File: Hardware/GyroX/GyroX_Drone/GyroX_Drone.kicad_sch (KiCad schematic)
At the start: 13 parts, among them J1 USB_C_Receptacle_USB2.0_16P, Q1 PMOS, U1 SPX3819M5-L-3-3

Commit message: USB-UART circuit designed
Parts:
- added C19, C20: 0.1uF, Capacitor_SMD:C_0603_1608Metric, symbol Device:C
- added R8, R9: 1k, Resistor_SMD:R_0603_1608Metric, symbol Device:R
- added U2: CH340K, Package_SO:SSOP-10-1EP_3.9x4.9mm_P1mm_EP2.1x3.3mm, symbol Interface_USB:CH340K
- added U3: 2N7002DW, 2N7002DW:SOT363, symbol 2N7002DW:2N7002DW
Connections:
- net +3.3V: now also C20.1, U2.7 (VCC)
- net D+: now also U2.1 (UD+)
- net D-: now also U2.2 (UD-)
- net GND: now also C19.2, C20.2, U2.11 (GND), U2.3 (GND)
- new net: R9.2, U2.9 (RXD)
- new net: R8.2, U2.8 (TXD)
- new net: C19.1, U2.10 (V3)
- new net DTR: U2.4 (~{DTR}), U3.2 (G1), U3.4 (S2)
- new net EN: U3.6 (D1)
- new net IO0: U3.3 (D2)
- new net RTS: U2.6 (~{RTS}), U3.1 (S1), U3.5 (G2)
- new net RX: R9.1
- new net TX: R8.1
- no-connect marks 2 -> 3
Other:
- note added: "USB - UART CIRCUIT"
- note added: "USB-C POWER IN CIRCUIT"

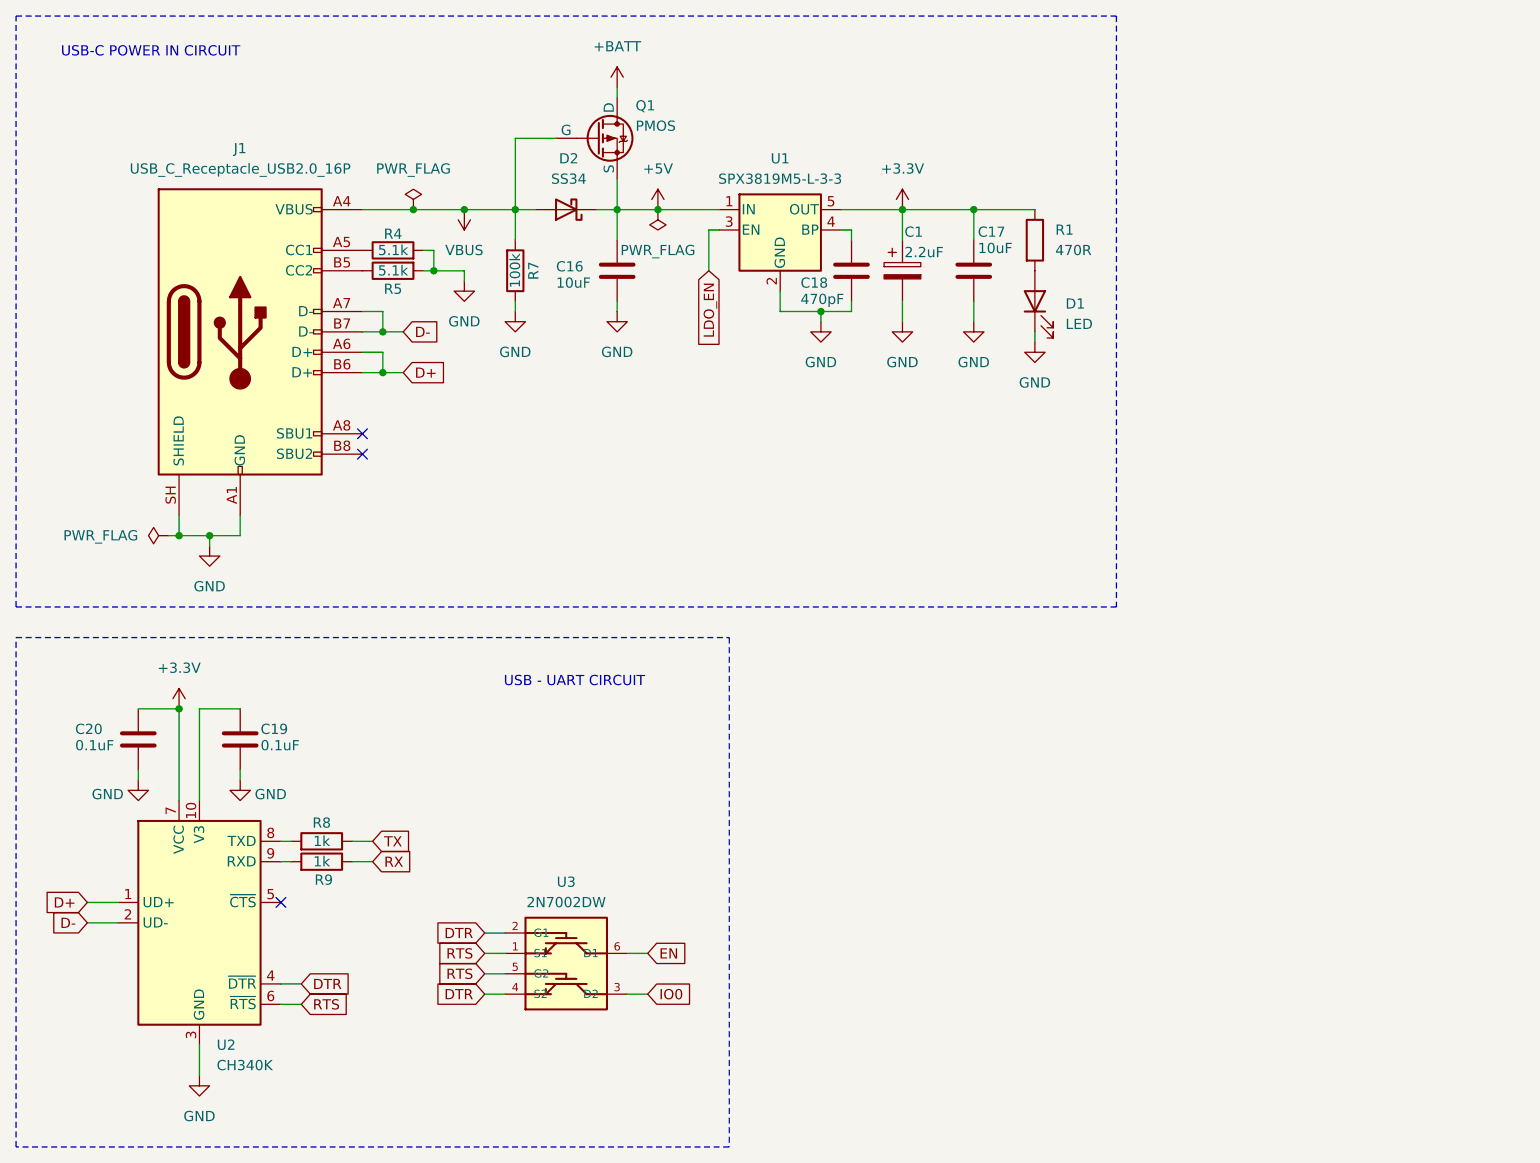
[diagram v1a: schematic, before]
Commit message: Battery charging circuit designed
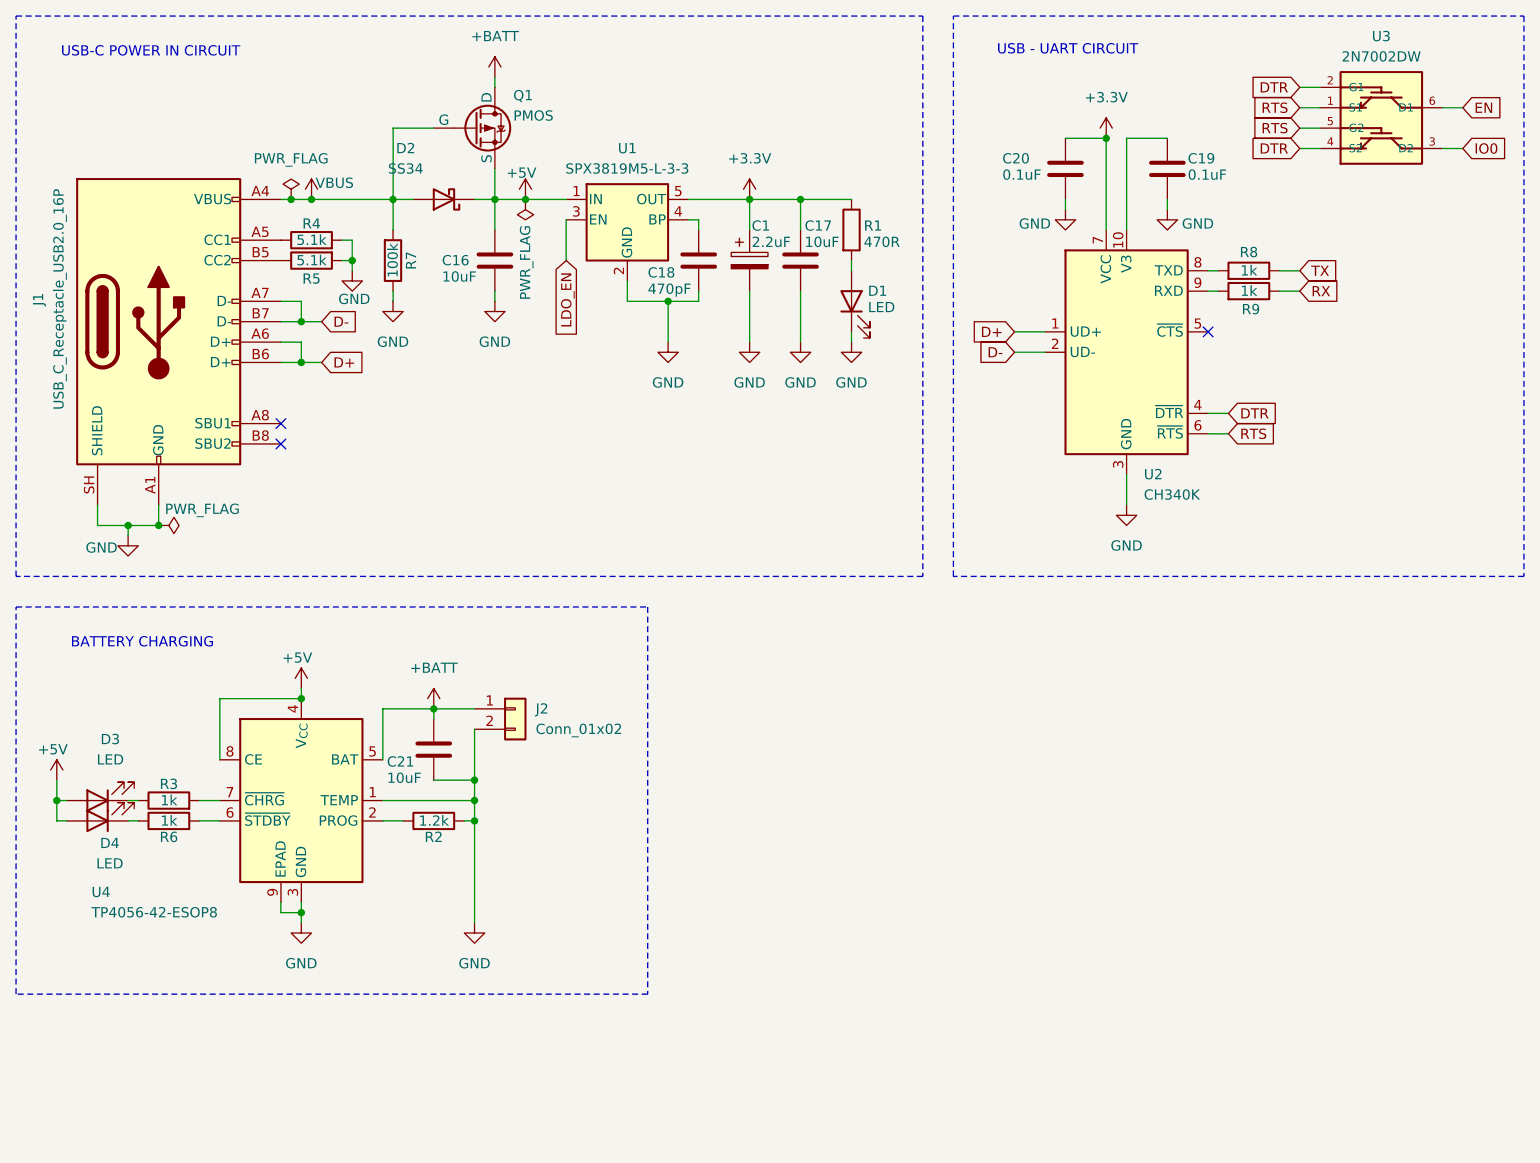
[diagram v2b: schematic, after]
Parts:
- added C21: 10uF, Capacitor_SMD:C_0603_1608Metric, symbol Device:C
- added D3, D4: LED, symbol Device:LED
- added J2: Conn_01x02, symbol Connector_Generic:Conn_01x02
- added R2: 1.2k, symbol Device:R
- added R3, R6: 1k, symbol Device:R
- added U4: TP4056-42-ESOP8, Package_SO:SOIC-8-1EP_3.9x4.9mm_P1.27mm_EP2.41x3.3mm_ThermalVias, symbol Battery_Management:TP4056-42-ESOP8
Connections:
- net +5V: now also D3.2 (A), D4.2 (A), U4.4 (V_{CC}), U4.8 (CE)
- net +BATT: now also C21.1, J2.1 (Pin_1), U4.5 (BAT)
- net GND: now also C21.2, J2.2 (Pin_2), R2.2, U4.1 (TEMP), U4.3 (GND), U4.9 (EPAD)
- new net: R2.1, U4.2 (PROG)
- new net: D3.1 (K), R3.1
- new net: R3.2, U4.7 (~{CHRG})
- new net: D4.1 (K), R6.1
- new net: R6.2, U4.6 (~{STDBY})
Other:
- note added: "BATTERY CHARGING"
- moved on the sheet: C1, C16, C17, C18, C19, C20, D1, D2, J1, Q1, R1, R4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

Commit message: MPU6050 IMU IC designed
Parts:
- added C22, C24: 0.1uF, Capacitor_SMD:C_0603_1608Metric, symbol Device:C
- added C23: 2.2nF, Capacitor_SMD:C_0603_1608Metric, symbol Device:C
- added C25: 10nF, Capacitor_SMD:C_0603_1608Metric, symbol Device:C
- added D5, D6, D7: LED, symbol Device:LED
- added R10, R11: 100k, Resistor_SMD:R_0603_1608Metric, symbol Device:R
- added R12, R13, R14: 1K, symbol Device:R
- added R15: 4.7k, symbol Device:R
- added R16, R17, R18: 10k, symbol Device:R
- added U5: MPU-6050, Sensor_Motion:InvenSense_QFN-24_4x4mm_P0.5mm, symbol Sensor_Motion:MPU-6050
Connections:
- net +3.3V: now also C24.1, C25.1, R16.1, R17.1, R18.1, U5.13 (VDD), U5.8 (VLOGIC)
- net +BATT: now also R10.1
- net GND: now also C22.2, C23.2, C24.2, C25.2, D5.1 (K), D6.1 (K), D7.1 (K), R11.2, R15.1, U5.1 (CLKIN), U5.11 (FSYNC), U5.18 (GND)
- new net: D5.2 (A), R12.2
- new net: C23.1, U5.20 (CPOUT)
- new net: R10.2, R11.1
- new net: R18.2, U5.24 (SDA)
- new net: D7.2 (A), R14.2
- new net: C22.1, U5.10 (REGOUT)
- new net: D6.2 (A), R13.2
- new net: R15.2, U5.9 (AD0)
- new net: R17.2, U5.23 (SCL)
- new net AUX_SCL: U5.7 (AUX_CL)
- new net AUX_SDA: U5.6 (AUX_DA)
- new net MPU_INT: R16.2, U5.12 (INT)
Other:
- note added: "DEBUGGING LEDS"
- note added: "MPU6050 IMU"

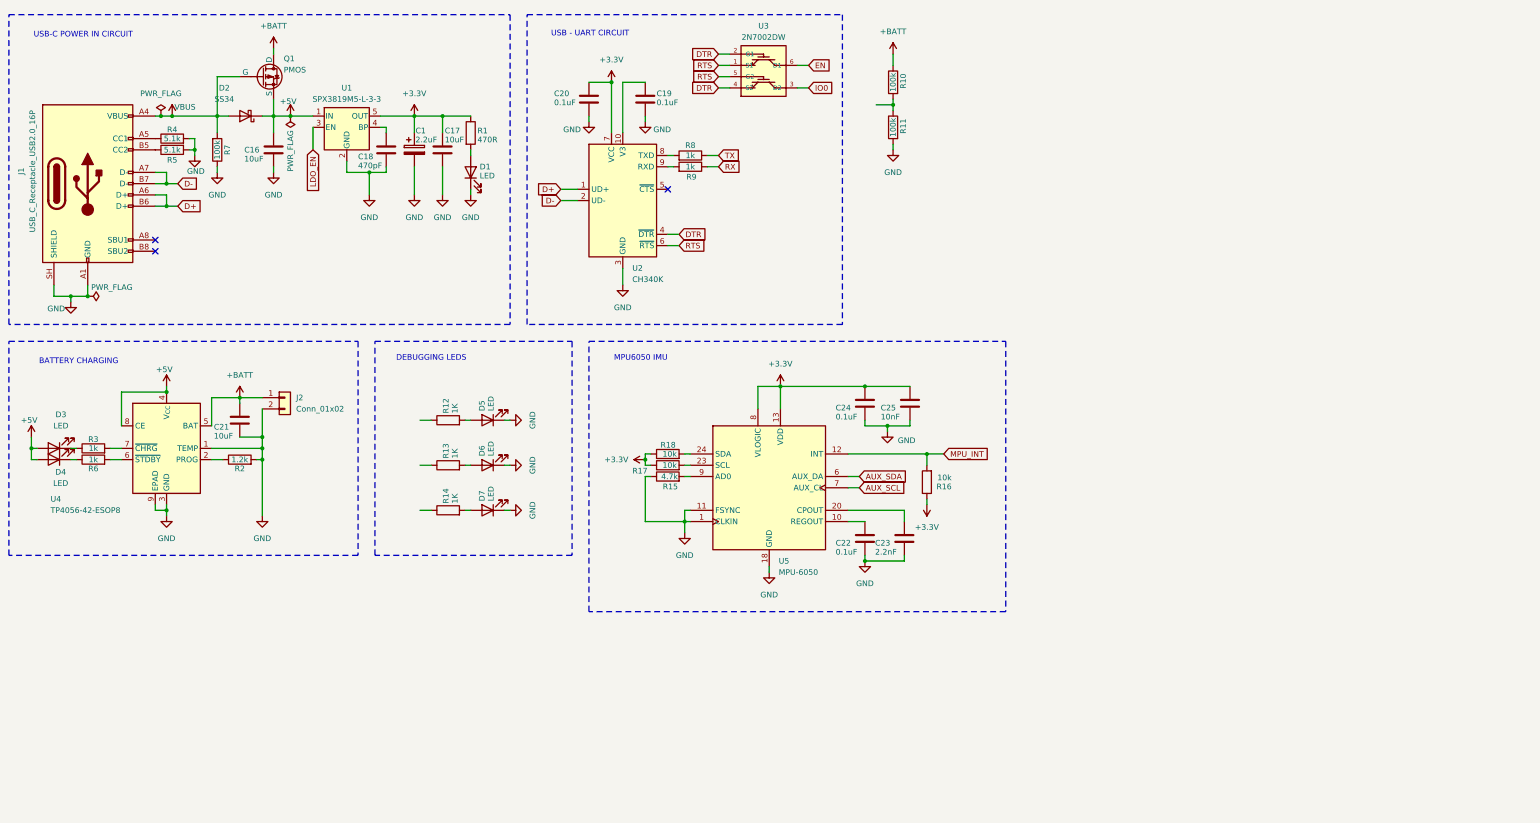
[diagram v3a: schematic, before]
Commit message: MCU and BMP390 sensor added
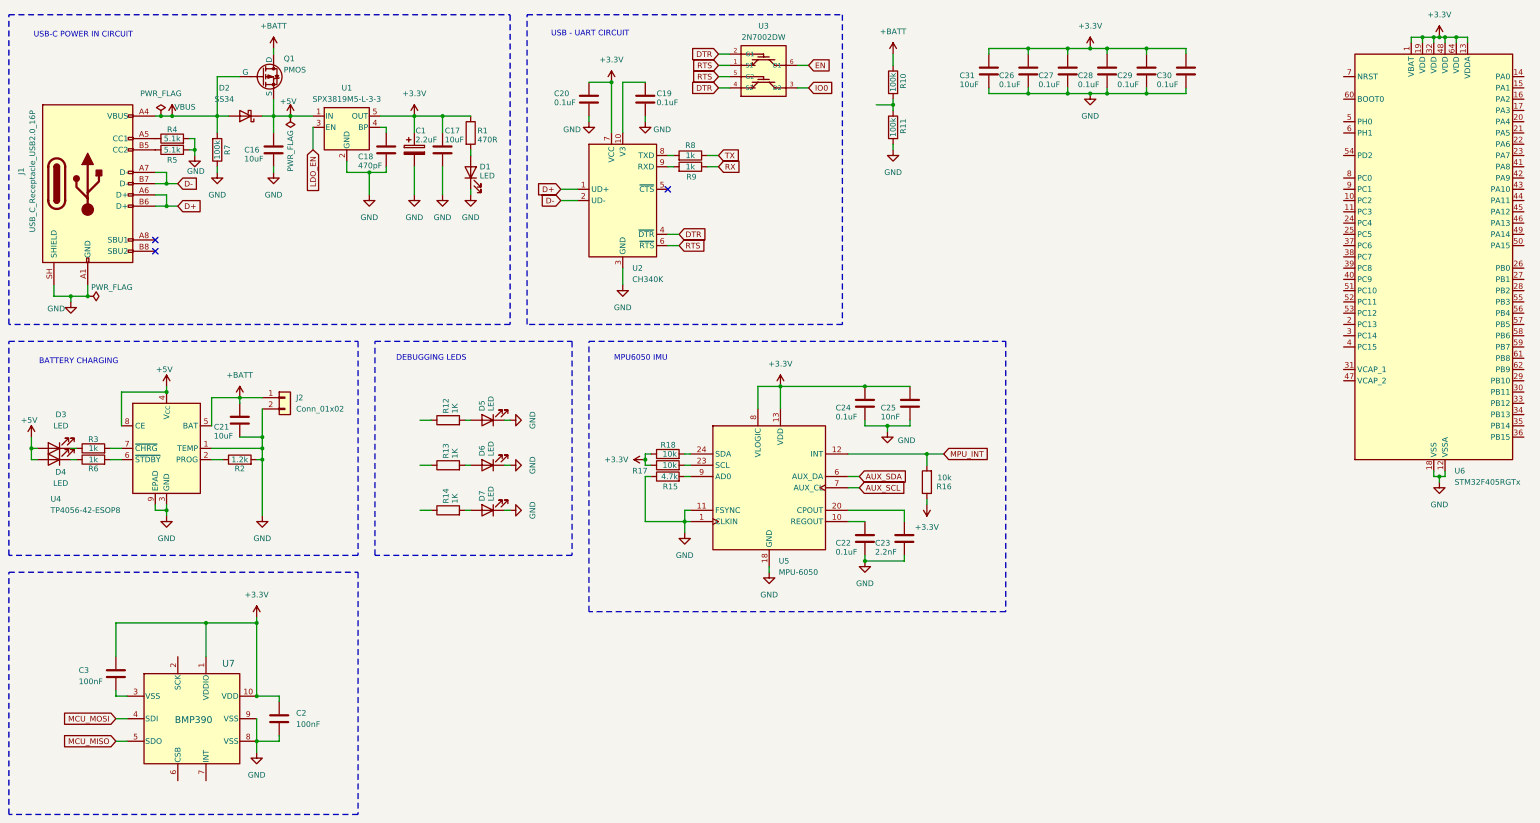
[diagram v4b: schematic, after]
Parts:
- added C2, C3: 100nF, symbol Device:C
- added C26, C27, C28, C29, C30: 0.1uF, Capacitor_SMD:C_0603_1608Metric, symbol Device:C
- added C31: 10uF, Capacitor_SMD:C_0603_1608Metric, symbol Device:C
- added U6: STM32F405RGTx, Package_QFP:LQFP-64_10x10mm_P0.5mm, symbol MCU_ST_STM32F4:STM32F405RGTx
- added U7: BMP390, 10LGA_2X2X0p75_BOS, symbol BMP390:BMP390
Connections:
- net +3.3V: now also C2.1, C26.1, C27.1, C28.1, C29.1, C3.1, C30.1, C31.1, U6.1 (VBAT), U6.13 (VDDA), U6.19 (VDD), U6.32 (VDD), U6.48 (VDD), U6.64 (VDD), U7.1 (VDDIO), U7.10 (VDD)
- net GND: now also C2.2, C26.2, C27.2, C28.2, C29.2, C30.2, C31.2, U6.12 (VSSA), U6.18 (VSS), U6.63 (VSS), U7.8 (VSS), U7.9 (VSS)
- new net: C3.2, U7.3 (VSS)
- new net MCU_MISO: U7.5 (SDO)
- new net MCU_MOSI: U7.4 (SDI)
